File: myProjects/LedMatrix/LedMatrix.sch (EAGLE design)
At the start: 9 parts, among them IC1 74HC595N, IC2 74HC595N, IC3 74HC595N, IC4 ULN2803, U1 RNET, U2 RNET, X1 INPUT, X2 OUTPUT

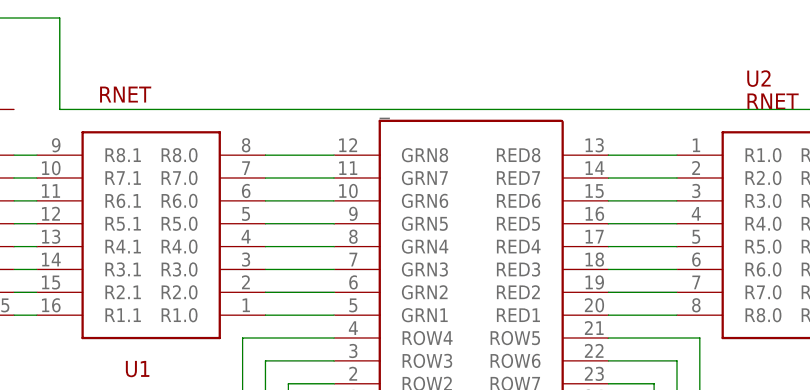
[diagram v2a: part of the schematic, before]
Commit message: fixed some labelling
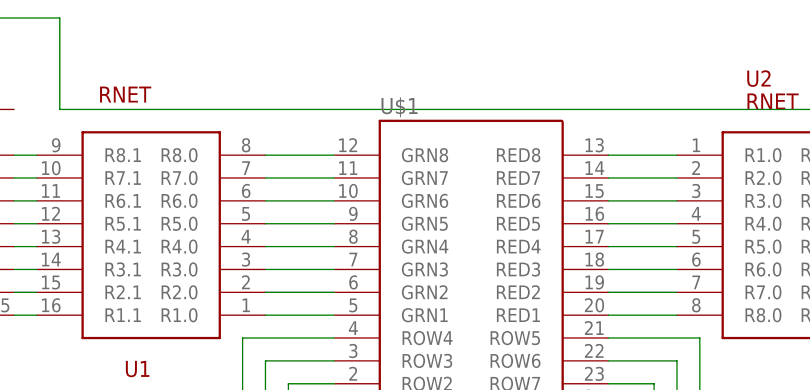
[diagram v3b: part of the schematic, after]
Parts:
- renumbered _ to U$1
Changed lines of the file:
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@@
 </classes>
 <parts>
-<part name="_" library="led-matrix-v2" deviceset="WLG-M2088A" device="/8EG" value=""/>
+<part name="U$1" library="led-matrix-v2" deviceset="WLG-M2088A" device="/8EG" value=""/>
 <part name="IC1" library="74xx-eu" deviceset="74*595" device="N" technology="HC"/>
 <part name="IC2" library="74xx-eu" deviceset="74*595" device="N" technology="HC"/>
@@
 </plain>
 <instances>
-<instance part="_" gate="G$1" x="93.98" y="69.85"/>
+<instance part="U$1" gate="G$1" x="93.98" y="69.85"/>
 <instance part="IC1" gate="A" x="30.48" y="76.2" rot="MR180"/>
 <instance part="IC2" gate="A" x="157.48" y="76.2" rot="R180"/>
@@
 <net name="N$9" class="0">
 <segment>
-<pinref part="_" gate="G$1" pin="GRN1"/>
+<pinref part="U$1" gate="G$1" pin="GRN1"/>
 <pinref part="U1" gate="G$1" pin="R1.0"/>
 <wire x1="71.12" y1="66.04" x2="78.74" y2="66.04" width="0.1524" layer="91"/>
@@
 <net name="N$10" class="0">
 <segment>
-<pinref part="_" gate="G$1" pin="GRN2"/>
+<pinref part="U$1" gate="G$1" pin="GRN2"/>
 <pinref part="U1" gate="G$1" pin="R2.0"/>
 <wire x1="71.12" y1="68.58" x2="78.74" y2="68.58" width="0.1524" layer="91"/>
@@
 <net name="N$11" class="0">
 <segment>
-<pinref part="_" gate="G$1" pin="GRN3"/>
+<pinref part="U$1" gate="G$1" pin="GRN3"/>
 <pinref part="U1" gate="G$1" pin="R3.0"/>
 <wire x1="71.12" y1="71.12" x2="78.74" y2="71.12" width="0.1524" layer="91"/>
@@
 <net name="N$12" class="0">
 <segment>
-<pinref part="_" gate="G$1" pin="GRN4"/>
+<pinref part="U$1" gate="G$1" pin="GRN4"/>
 <pinref part="U1" gate="G$1" pin="R4.0"/>
 <wire x1="71.12" y1="73.66" x2="78.74" y2="73.66" width="0.1524" layer="91"/>
@@
 <net name="N$13" class="0">
 <segment>
-<pinref part="_" gate="G$1" pin="GRN5"/>
+<pinref part="U$1" gate="G$1" pin="GRN5"/>
 <pinref part="U1" gate="G$1" pin="R5.0"/>
 <wire x1="71.12" y1="76.2" x2="78.74" y2="76.2" width="0.1524" layer="91"/>
@@
 <net name="N$14" class="0">
 <segment>
-<pinref part="_" gate="G$1" pin="GRN6"/>
+<pinref part="U$1" gate="G$1" pin="GRN6"/>
 <pinref part="U1" gate="G$1" pin="R6.0"/>
 <wire x1="71.12" y1="78.74" x2="78.74" y2="78.74" width="0.1524" layer="91"/>
@@
 <net name="N$15" class="0">
 <segment>
-<pinref part="_" gate="G$1" pin="GRN7"/>
+<pinref part="U$1" gate="G$1" pin="GRN7"/>
 <pinref part="U1" gate="G$1" pin="R7.0"/>
 <wire x1="71.12" y1="81.28" x2="78.74" y2="81.28" width="0.1524" layer="91"/>
@@
 <net name="N$16" class="0">
 <segment>
-<pinref part="_" gate="G$1" pin="GRN8"/>
+<pinref part="U$1" gate="G$1" pin="GRN8"/>
 <pinref part="U1" gate="G$1" pin="R8.0"/>
 <wire x1="71.12" y1="83.82" x2="78.74" y2="83.82" width="0.1524" layer="91"/>
@@
 <net name="N$17" class="0">
 <segment>
-<pinref part="_" gate="G$1" pin="RED8"/>
+<pinref part="U$1" gate="G$1" pin="RED8"/>
 <pinref part="U2" gate="G$1" pin="R1.0"/>
 <wire x1="116.84" y1="83.82" x2="109.22" y2="83.82" width="0.1524" layer="91"/>
@@
 <net name="N$18" class="0">
 <segment>
-<pinref part="_" gate="G$1" pin="RED7"/>
+<pinref part="U$1" gate="G$1" pin="RED7"/>
 <pinref part="U2" gate="G$1" pin="R2.0"/>
 <wire x1="116.84" y1="81.28" x2="109.22" y2="81.28" width="0.1524" layer="91"/>
@@
 <net name="N$19" class="0">
 <segment>
-<pinref part="_" gate="G$1" pin="RED6"/>
+<pinref part="U$1" gate="G$1" pin="RED6"/>
 <pinref part="U2" gate="G$1" pin="R3.0"/>
 <wire x1="116.84" y1="78.74" x2="109.22" y2="78.74" width="0.1524" layer="91"/>
@@
 <net name="N$20" class="0">
 <segment>
-<pinref part="_" gate="G$1" pin="RED5"/>
+<pinref part="U$1" gate="G$1" pin="RED5"/>
 <pinref part="U2" gate="G$1" pin="R4.0"/>
 <wire x1="116.84" y1="76.2" x2="109.22" y2="76.2" width="0.1524" layer="91"/>
@@
 <net name="N$21" class="0">
 <segment>
-<pinref part="_" gate="G$1" pin="RED4"/>
+<pinref part="U$1" gate="G$1" pin="RED4"/>
 <pinref part="U2" gate="G$1" pin="R5.0"/>
 <wire x1="116.84" y1="73.66" x2="109.22" y2="73.66" width="0.1524" layer="91"/>
@@
 <net name="N$22" class="0">
 <segment>
-<pinref part="_" gate="G$1" pin="RED3"/>
+<pinref part="U$1" gate="G$1" pin="RED3"/>
 <pinref part="U2" gate="G$1" pin="R6.0"/>
 <wire x1="116.84" y1="71.12" x2="109.22" y2="71.12" width="0.1524" layer="91"/>
@@
 <net name="N$23" class="0">
 <segment>
-<pinref part="_" gate="G$1" pin="RED2"/>
+<pinref part="U$1" gate="G$1" pin="RED2"/>
 <pinref part="U2" gate="G$1" pin="R7.0"/>
 <wire x1="116.84" y1="68.58" x2="109.22" y2="68.58" width="0.1524" layer="91"/>
@@
 <net name="N$24" class="0">
 <segment>
-<pinref part="_" gate="G$1" pin="RED1"/>
+<pinref part="U$1" gate="G$1" pin="RED1"/>
 <pinref part="U2" gate="G$1" pin="R8.0"/>
 <wire x1="116.84" y1="66.04" x2="109.22" y2="66.04" width="0.1524" layer="91"/>
@@
 <wire x1="66.04" y1="38.1" x2="76.2" y2="38.1" width="0.1524" layer="91"/>
 <wire x1="76.2" y1="38.1" x2="76.2" y2="55.88" width="0.1524" layer="91"/>
-<pinref part="_" gate="G$1" pin="ROW1"/>
+<pinref part="U$1" gate="G$1" pin="ROW1"/>
 <wire x1="76.2" y1="55.88" x2="78.74" y2="55.88" width="0.1524" layer="91"/>
 </segment>
@@
 <wire x1="66.04" y1="35.56" x2="73.66" y2="35.56" width="0.1524" layer="91"/>
 <wire x1="73.66" y1="35.56" x2="73.66" y2="58.42" width="0.1524" layer="91"/>
-<pinref part="_" gate="G$1" pin="ROW2"/>
+<pinref part="U$1" gate="G$1" pin="ROW2"/>
 <wire x1="73.66" y1="58.42" x2="78.74" y2="58.42" width="0.1524" layer="91"/>
 </segment>
@@
 <wire x1="66.04" y1="33.02" x2="71.12" y2="33.02" width="0.1524" layer="91"/>
 <wire x1="71.12" y1="33.02" x2="71.12" y2="60.96" width="0.1524" layer="91"/>
-<pinref part="_" gate="G$1" pin="ROW3"/>
+<pinref part="U$1" gate="G$1" pin="ROW3"/>
 <wire x1="71.12" y1="60.96" x2="78.74" y2="60.96" width="0.1524" layer="91"/>
 </segment>
@@
 <wire x1="66.04" y1="30.48" x2="68.58" y2="30.48" width="0.1524" layer="91"/>
 <wire x1="68.58" y1="30.48" x2="68.58" y2="63.5" width="0.1524" layer="91"/>
-<pinref part="_" gate="G$1" pin="ROW4"/>
+<pinref part="U$1" gate="G$1" pin="ROW4"/>
 <wire x1="68.58" y1="63.5" x2="78.74" y2="63.5" width="0.1524" layer="91"/>
 </segment>
@@
 <wire x1="66.04" y1="27.94" x2="119.38" y2="27.94" width="0.1524" layer="91"/>
 <wire x1="119.38" y1="27.94" x2="119.38" y2="63.5" width="0.1524" layer="91"/>
-<pinref part="_" gate="G$1" pin="ROW5"/>
+<pinref part="U$1" gate="G$1" pin="ROW5"/>
 <wire x1="119.38" y1="63.5" x2="109.22" y2="63.5" width="0.1524" layer="91"/>
 </segment>
@@
 <wire x1="66.04" y1="25.4" x2="116.84" y2="25.4" width="0.1524" layer="91"/>
 <wire x1="116.84" y1="25.4" x2="116.84" y2="60.96" width="0.1524" layer="91"/>
-<pinref part="_" gate="G$1" pin="ROW6"/>
+<pinref part="U$1" gate="G$1" pin="ROW6"/>
 <wire x1="116.84" y1="60.96" x2="109.22" y2="60.96" width="0.1524" layer="91"/>
 </segment>
@@
 <wire x1="66.04" y1="22.86" x2="114.3" y2="22.86" width="0.1524" layer="91"/>
 <wire x1="114.3" y1="22.86" x2="114.3" y2="58.42" width="0.1524" layer="91"/>
-<pinref part="_" gate="G$1" pin="ROW7"/>
+<pinref part="U$1" gate="G$1" pin="ROW7"/>
 <wire x1="114.3" y1="58.42" x2="109.22" y2="58.42" width="0.1524" layer="91"/>
 </segment>
@@
 <wire x1="66.04" y1="20.32" x2="111.76" y2="20.32" width="0.1524" layer="91"/>
 <wire x1="111.76" y1="20.32" x2="111.76" y2="55.88" width="0.1524" layer="91"/>
-<pinref part="_" gate="G$1" pin="ROW8"/>
+<pinref part="U$1" gate="G$1" pin="ROW8"/>
 <wire x1="111.76" y1="55.88" x2="109.22" y2="55.88" width="0.1524" layer="91"/>
 </segment>
